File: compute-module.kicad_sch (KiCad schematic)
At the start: 99 parts, among them J1 DF40HC(3.0)-100DS-0.4v, J2 DF40HC(3.0)-100DS-0.4v, M1 compute-module-4-1.5mm

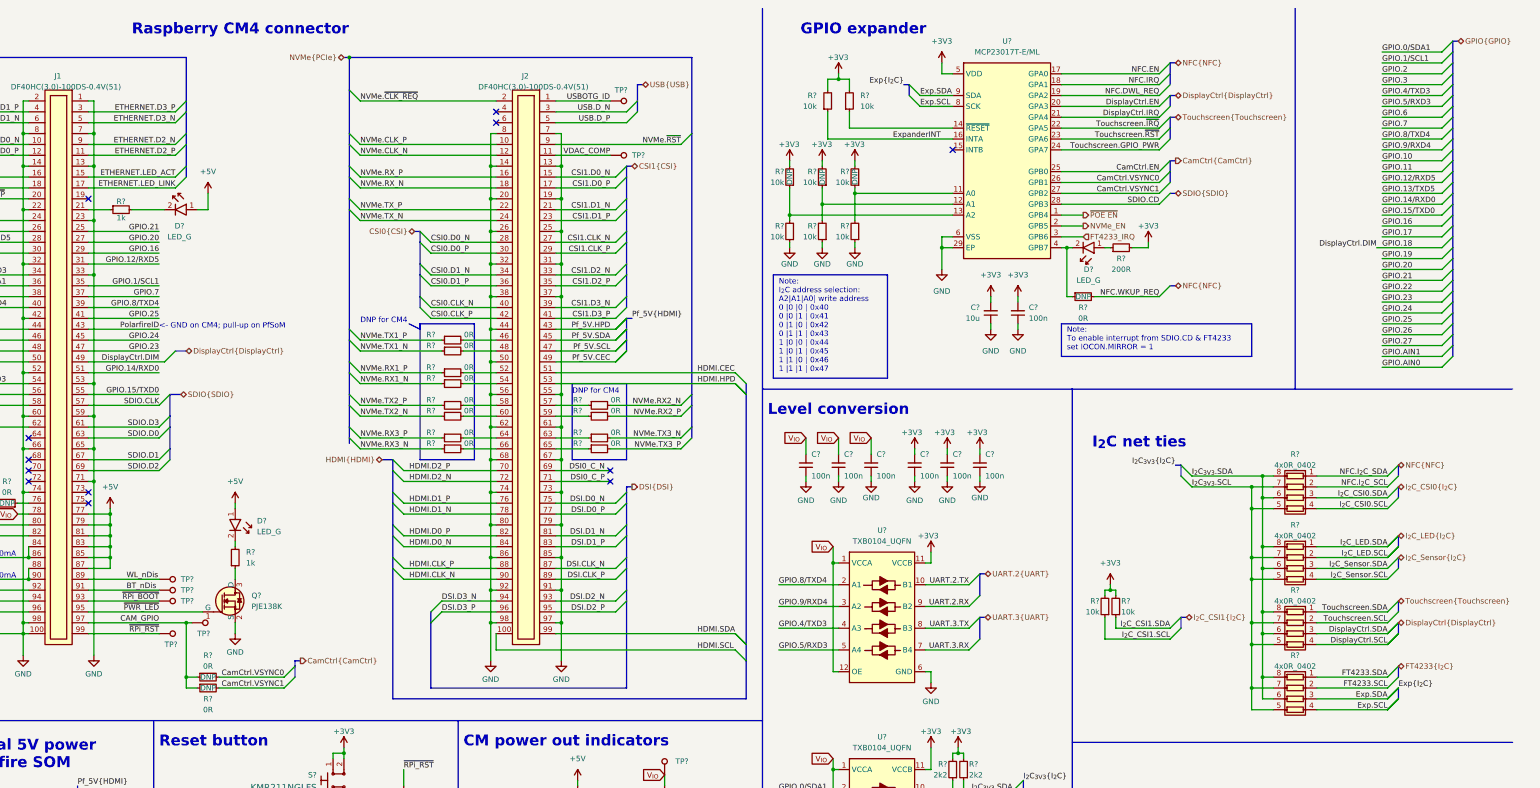
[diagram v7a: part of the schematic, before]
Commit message: [#54617] Move LVDS display related components to separate repo
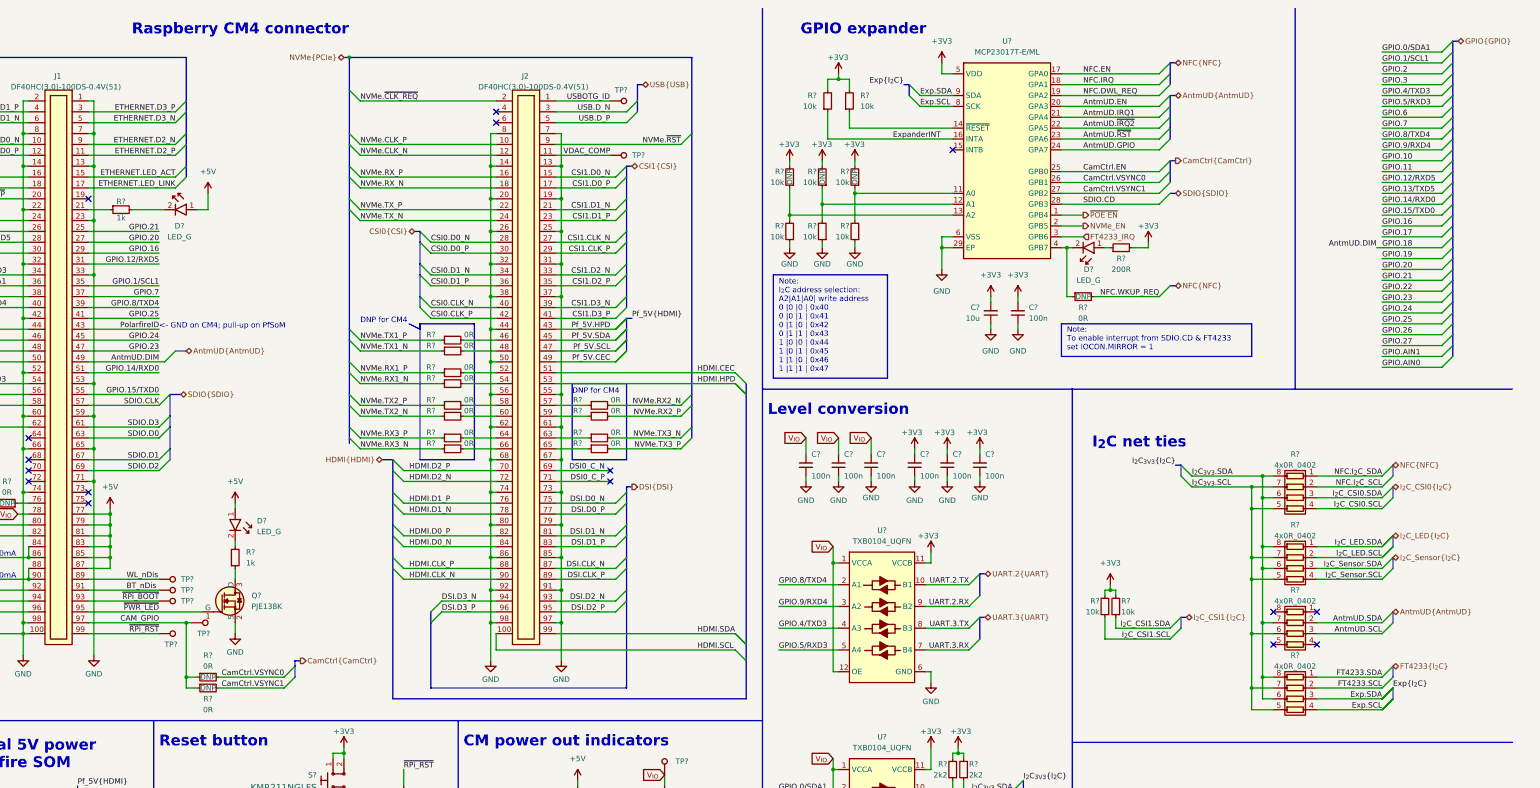
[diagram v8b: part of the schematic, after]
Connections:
- net I_{2}C_{3V3}.SCL: now also R?.6 (R3.2); no longer R?.5 (R4.2), R?.7 (R2.2)
- net I_{2}C_{3V3}.SDA: now also R?.7 (R2.2); no longer R?.6 (R3.2), R?.8 (R1.2)
- net DisplayCtrl.DIM renamed AntmUD.DIM
- net DisplayCtrl.EN renamed AntmUD.EN
- net DisplayCtrl.IRQ renamed AntmUD.IRQ1
- net DisplayCtrl.SCL: no longer names the net of R?.4 (R4.1)
- net DisplayCtrl.SDA renamed AntmUD.SCL
- net Touchscreen.GPIO_PWR renamed AntmUD.GPIO
- net Touchscreen.SCL renamed AntmUD.SDA
- net Touchscreen.SDA: no longer names the net of R?.1 (R1.1)
- net Touchscreen.~{IRQ} renamed AntmUD.~{IRQ2}
- net Touchscreen.~{RST} renamed AntmUD.~{RST}
- no-connect marks 12 -> 16
